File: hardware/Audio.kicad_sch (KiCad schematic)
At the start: 48 parts, among them IC301 LM4991xx, J301 CAT_TX, J302 CAT_RX, Q301 IRLML2060, Q302 BSS138, Q303 BSS138, U301 MCP6002, U302 MAX9814

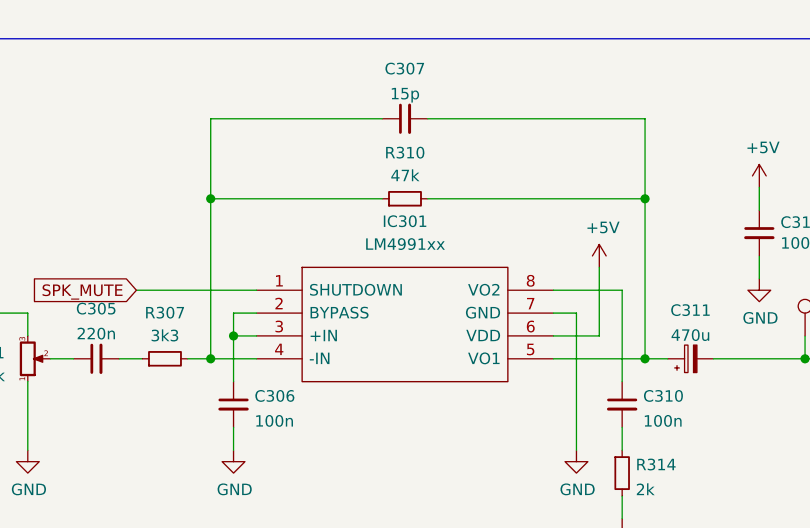
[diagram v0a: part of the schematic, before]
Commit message: Updated some components values
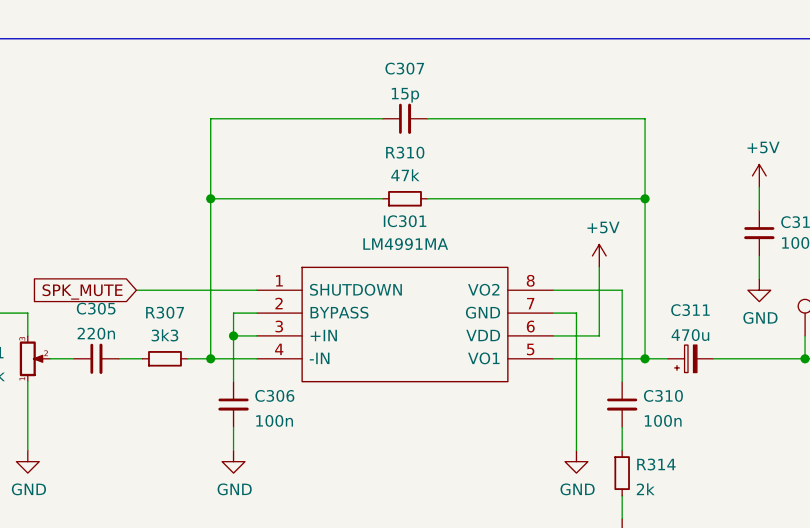
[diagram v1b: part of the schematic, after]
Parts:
- IC301: value LM4991xx -> LM4991MA
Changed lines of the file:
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@@
       (effects (font (size 1.27 1.27)))
     )
-    (property "Value" "LM4991xx" (at 152.4 41.91 0)
+    (property "Value" "LM4991MA" (at 152.4 41.91 0)
       (effects (font (size 1.27 1.27)))
     )
